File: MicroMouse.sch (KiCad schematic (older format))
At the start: 76 parts, among them CN11 mouseBattery, Q1 IRLML6402, Q2 IRLML6344, SW1 SPST, SW2 SPST, SW3 SPST, U1 FULL_LED_A, U2 STM32F405RGTx, U3 TB6612, U4 CN_MOTOR, U5 CN_MOTOR, U6 MPU9250, U7 ZH

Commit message: とりあえずコミット
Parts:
- removed R10, R9: 10, Resistors_SMD:R_0603_HandSoldering, symbol R
- removed R11: 60.4, Resistors_SMD:R_0603_HandSoldering, symbol R
- removed U1: FULL_LED_A, myfootprint:OSTAMA5B31A, symbol FULL_LED_A
- removed U6: MPU9250, myfootprint:FH-1x5SG, symbol MPU9250
- removed U7: ZH, myfootprint:B6B-ZR, symbol ZH
- added C18, C19, C20, C21: 0.1u, Resistors_SMD:R_0603_HandSoldering, symbol C
- added D1, D2: LED, Resistors_SMD:R_0603_HandSoldering, symbol LED-RESCUE-MicroMouse
- added R2, R3: 280, Resistors_SMD:R_0603_HandSoldering, symbol R
- added U1: 3p, Pin_Headers:Pin_Header_Straight_1x03, symbol 3p
- added U6: 4p, Pin_Headers:Pin_Header_Straight_1x04, symbol 4p
- added U7: icm_left, Pin_Headers:Pin_Header_Straight_1x04, symbol icm_left
- added U8: icm_right, Pin_Headers:Pin_Header_Straight_1x04, symbol icm_right
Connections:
- net labels added: CS, DBG_LED_4, DBG_LED_5, SDO
- net labels removed: Mode_LED_1, Mode_LED_2, Mode_LED_3
- wire segments 289 -> 302
- no-connect marks 28 -> 25
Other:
- note added: "DBG_LED(Orange)"
- note added: "MCU VDD"
- note added: "REG 3.3V"
- note removed: "B"
- note removed: "DBG_LED"
- note removed: "G"
- note removed: "Mode_LED"
- note removed: "O"
- note removed: "Power_IMU"
- note removed: "R"
- note removed: "Y"
- note removed: "YG"
- moved on the sheet: C1, C15, C16, C17, C2, C3, C4, C5, C6, CN11, D13, D5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

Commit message: GNDの配線だけした
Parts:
- removed U7: icm_left, Pin_Headers:Pin_Header_Straight_1x04, symbol icm_left
- removed U8: icm_right, Pin_Headers:Pin_Header_Straight_1x04, symbol icm_right
- added C22: 4.7u, Resistors_SMD:R_0603_HandSoldering, symbol C
- added U7: ICM-20602, myfootprint:ICM-20602, symbol ICM-20602
- C12, C3, C6: footprint myfootprint:EEEHC1E470XP -> Capacitors_SMD:c_elec_6.3x7.7
- CN11: footprint myfootprint:DF3A-2P-2DSA -> RP_KiCAD_Connector:XA_2T
- OPAMP1, OPAMP2: footprint myfootprint:AD8532AR -> Housings_SOIC:SOIC-8_3.9x4.9mm_Pitch1.27mm
- Q1, Q2: footprint myfootprint:IRLML6402 -> myfootprint:SOT-23_Handsoldering
- REG1, REG2: footprint myfootprint:AZ1086 -> TO_SOT_Packages_SMD:SOT-223_reg
- SEN1, SEN2, SEN3, SEN4: footprint myfootprint:TSL262-R-LF-ND -> myfootprint:Socket_Strip_Straight_1x03
- U2: footprint myfootprint:STM32F405RGT6 -> myfootprint:LQFP-64_10x10mm_Pitch0.5mm
- U3: footprint myfootprint:TB6612FNG -> Housings_SSOP:SSOP-24_5.3x8.2mm_Pitch0.65mm
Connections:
- net +3V3: now also C22.1, U7.1 (VDD)
- net CS: now also U7.8 (CS)
- net GND: now also C22.2, U7.5 (GND), U7.7 (NC)
- net SCL: now also U7.2 (SCL/SPC)
- net SDA: now also U7.3 (SDA/SDI)
- net SDO: now also U7.4 (SA0/SDO)

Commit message: 昔の確認
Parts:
- removed C15, C16: 47u, Resistors_SMD:R_1210_HandSoldering, symbol C
- removed C17: 0.1u, Resistors_SMD:R_0603_HandSoldering, symbol C
- removed C3, C6: 47u, Capacitors_SMD:c_elec_6.3x7.7, symbol CP
- added C19: 10u, Resistors_SMD:R_0603_HandSoldering, symbol C
- added C3: 22u, Resistors_SMD:R_0603_HandSoldering, symbol C
- C1, C2: value 47u -> 10u; footprint Resistors_SMD:R_1210_HandSoldering -> Resistors_SMD:R_0603_HandSoldering
- C4: value 47u -> 22u; footprint Resistors_SMD:R_1210_HandSoldering -> Resistors_SMD:R_0603_HandSoldering
- C5: value 47u -> 0.1u; footprint Resistors_SMD:R_1210_HandSoldering -> Resistors_SMD:R_0603_HandSoldering
- renumbered C22 to C10, C7 to C11, C8 to C12, C9 to C13, C10 to C14, C11 to C15, C12 to C16, C13 to C17, C14 to C18, C18 to C6, C19 to C7, C20 to C8, C21 to C9, CN11 to CN1, D5 to D1, D11 to D10, D12 to D11, D6 to D2, D7 to D3, D1 to D4, D2 to D5, D13 to D6, D8 to D7, D9 to D8, D10 to D9, R13 to R10, R15 to R11, R16 to R12, R17 to R13, R18 to R14, R19 to R15, R20 to R16, R21 to R17, R22 to R18, R23 to R19, R6 to R2, R24 to R20, R25 to R21, R26 to R22, R27 to R23, R29 to R24, R28 to R25, R31 to R26, R32 to R27, R7 to R3, R8 to R4, R2 to R5, R3 to R6, R30 to R7, R12 to R8, R14 to R9, U2 to U1, U3 to U2, U4 to U3, U5 to U4, U1 to U5, U7 to U6, U6 to U7
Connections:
- net +3V3: now also C4.1, C5.1, C19.1
- net +5V: now also C3.1; no longer C4.1, C5.1
- net GND: now also C19.2, C3.2

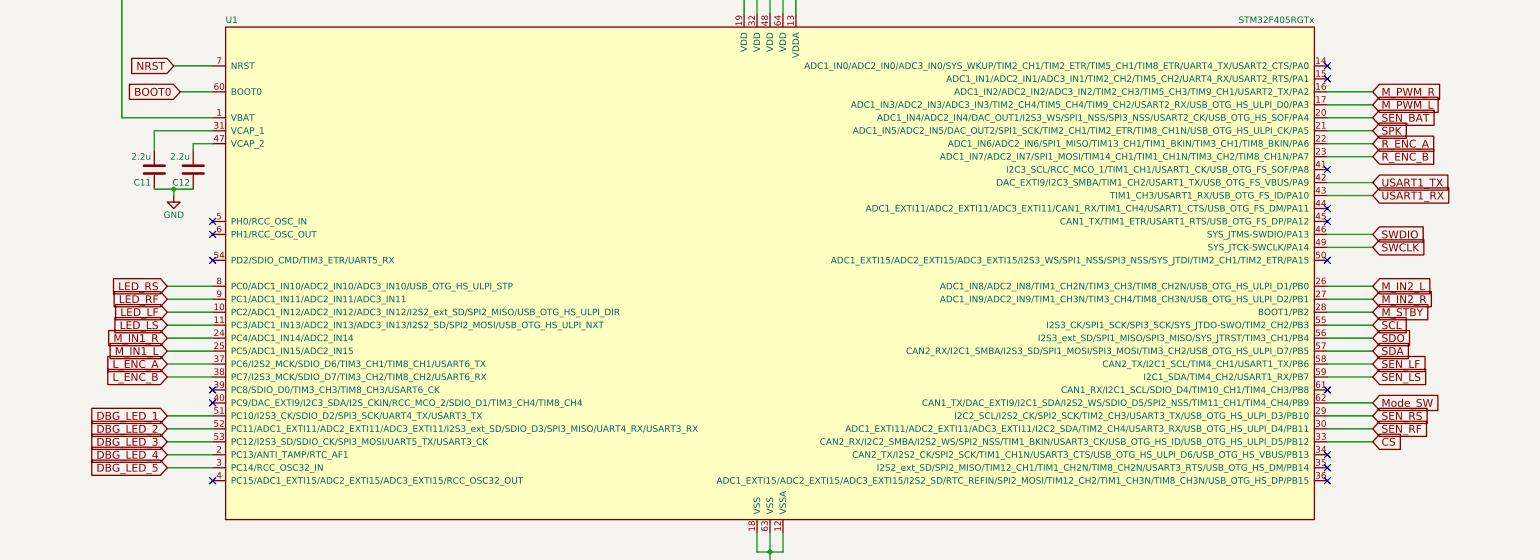
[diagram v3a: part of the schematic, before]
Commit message: stmのピン変え
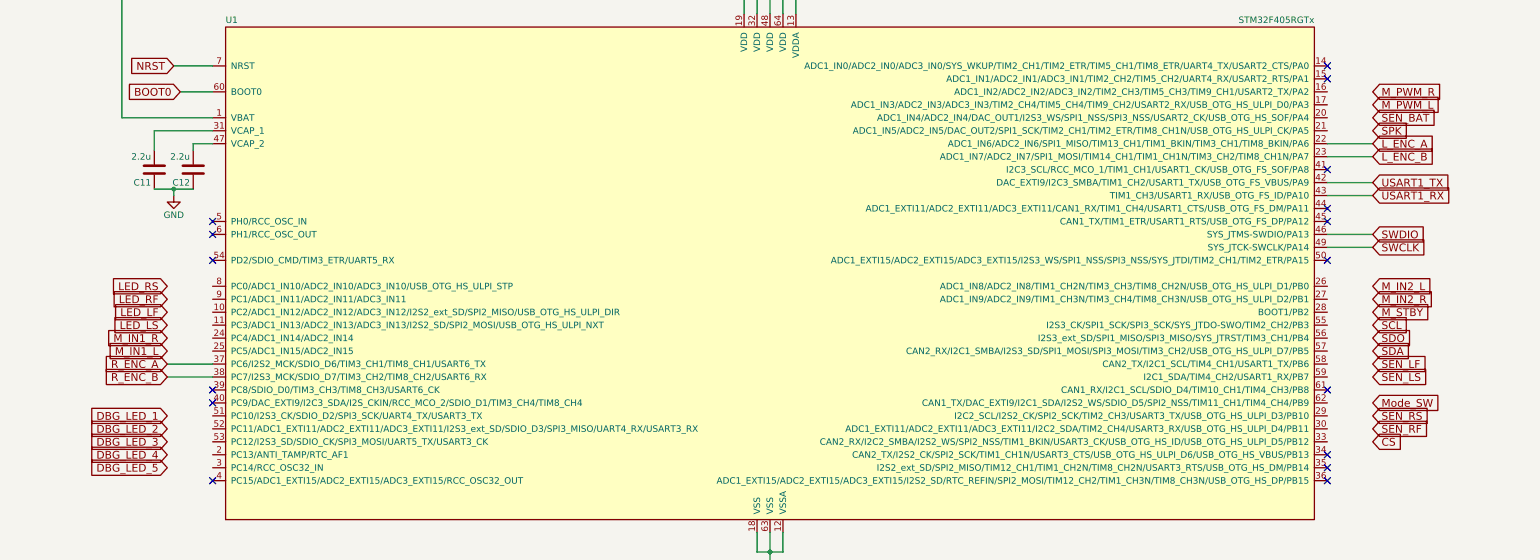
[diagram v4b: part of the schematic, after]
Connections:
- net CS: no longer U1.33 (CAN2_RX/I2C2_SMBA/I2S2_WS/SPI2_NSS/TIM1_BKIN/USART3_CK/USB_OTG_HS_ID/USB_OTG_HS_ULPI_D5/PB12)
- net DBG_LED_1: no longer U1.51 (PC10/I2S3_CK/SDIO_D2/SPI3_SCK/UART4_TX/USART3_TX)
- net DBG_LED_2: no longer U1.52 (PC11/ADC1_EXTI11/ADC2_EXTI11/ADC3_EXTI11/I2S3_ext_SD/SDIO_D3/SPI3_MISO/UART4_RX/USART3_RX)
- net DBG_LED_3: no longer U1.53 (PC12/I2S3_SD/SDIO_CK/SPI3_MOSI/UART5_TX/USART3_CK)
- net DBG_LED_4: no longer U1.2 (PC13/ANTI_TAMP/RTC_AF1)
- net DBG_LED_5: no longer U1.3 (PC14/RCC_OSC32_IN)
- net LED_LF: no longer U1.10 (PC2/ADC1_IN12/ADC2_IN12/ADC3_IN12/I2S2_ext_SD/SPI2_MISO/USB_OTG_HS_ULPI_DIR)
- net LED_LS: no longer U1.11 (PC3/ADC1_IN13/ADC2_IN13/ADC3_IN13/I2S2_SD/SPI2_MOSI/USB_OTG_HS_ULPI_NXT)
- net LED_RF: no longer U1.9 (PC1/ADC1_IN11/ADC2_IN11/ADC3_IN11)
- net LED_RS: no longer U1.8 (PC0/ADC1_IN10/ADC2_IN10/ADC3_IN10/USB_OTG_HS_ULPI_STP)
- net L_ENC_A: now also U1.22 (ADC1_IN6/ADC2_IN6/SPI1_MISO/TIM13_CH1/TIM1_BKIN/TIM3_CH1/TIM8_BKIN/PA6); no longer U1.37 (PC6/I2S2_MCK/SDIO_D6/TIM3_CH1/TIM8_CH1/USART6_TX)
- net L_ENC_B: now also U1.23 (ADC1_IN7/ADC2_IN7/SPI1_MOSI/TIM14_CH1/TIM1_CH1N/TIM3_CH2/TIM8_CH1N/PA7); no longer U1.38 (PC7/I2S3_MCK/SDIO_D7/TIM3_CH2/TIM8_CH2/USART6_RX)
- net M_IN1_L: no longer U1.25 (PC5/ADC1_IN15/ADC2_IN15)
- net M_IN1_R: no longer U1.24 (PC4/ADC1_IN14/ADC2_IN14)
- net M_IN2_L: no longer U1.26 (ADC1_IN8/ADC2_IN8/TIM1_CH2N/TIM3_CH3/TIM8_CH2N/USB_OTG_HS_ULPI_D1/PB0)
- net M_IN2_R: no longer U1.27 (ADC1_IN9/ADC2_IN9/TIM1_CH3N/TIM3_CH4/TIM8_CH3N/USB_OTG_HS_ULPI_D2/PB1)
- net M_PWM_L: no longer U1.17 (ADC1_IN3/ADC2_IN3/ADC3_IN3/TIM2_CH4/TIM5_CH4/TIM9_CH2/USART2_RX/USB_OTG_HS_ULPI_D0/PA3)
- net M_PWM_R: no longer U1.16 (ADC1_IN2/ADC2_IN2/ADC3_IN2/TIM2_CH3/TIM5_CH3/TIM9_CH1/USART2_TX/PA2)
- net M_STBY: no longer U1.28 (BOOT1/PB2)
- net Mode_SW: no longer U1.62 (CAN1_TX/DAC_EXTI9/I2C1_SDA/I2S2_WS/SDIO_D5/SPI2_NSS/TIM11_CH1/TIM4_CH4/PB9)
- net R_ENC_A: now also U1.37 (PC6/I2S2_MCK/SDIO_D6/TIM3_CH1/TIM8_CH1/USART6_TX); no longer U1.22 (ADC1_IN6/ADC2_IN6/SPI1_MISO/TIM13_CH1/TIM1_BKIN/TIM3_CH1/TIM8_BKIN/PA6)
- net R_ENC_B: now also U1.38 (PC7/I2S3_MCK/SDIO_D7/TIM3_CH2/TIM8_CH2/USART6_RX); no longer U1.23 (ADC1_IN7/ADC2_IN7/SPI1_MOSI/TIM14_CH1/TIM1_CH1N/TIM3_CH2/TIM8_CH1N/PA7)
- net SCL: no longer U1.55 (I2S3_CK/SPI1_SCK/SPI3_SCK/SYS_JTDO-SWO/TIM2_CH2/PB3)
- net SDA: no longer U1.57 (CAN2_RX/I2C1_SMBA/I2S3_SD/SPI1_MOSI/SPI3_MOSI/TIM3_CH2/USB_OTG_HS_ULPI_D7/PB5)
- net SDO: no longer U1.56 (I2S3_ext_SD/SPI1_MISO/SPI3_MISO/SYS_JTRST/TIM3_CH1/PB4)
- net SEN_BAT: no longer U1.20 (ADC1_IN4/ADC2_IN4/DAC_OUT1/I2S3_WS/SPI1_NSS/SPI3_NSS/USART2_CK/USB_OTG_HS_SOF/PA4)
- net SEN_LF: no longer U1.58 (CAN2_TX/I2C1_SCL/TIM4_CH1/USART1_TX/PB6)
- net SEN_LS: no longer U1.59 (I2C1_SDA/TIM4_CH2/USART1_RX/PB7)
- net SEN_RF: no longer U1.30 (ADC1_EXTI11/ADC2_EXTI11/ADC3_EXTI11/I2C2_SDA/TIM2_CH4/USART3_RX/USB_OTG_HS_ULPI_D4/PB11)
- net SEN_RS: no longer U1.29 (I2C2_SCL/I2S2_CK/SPI2_SCK/TIM2_CH3/USART3_TX/USB_OTG_HS_ULPI_D3/PB10)
- net SPK: no longer U1.21 (ADC1_IN5/ADC2_IN5/DAC_OUT2/SPI1_SCK/TIM2_CH1/TIM2_ETR/TIM8_CH1N/USB_OTG_HS_ULPI_CK/PA5)
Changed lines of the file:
@@
 	1    0    0    -1
 $EndComp
+Text GLabel 9050 4800 0    60   Input ~ 0
+R_ENC_A
+Text GLabel 9050 4900 0    60   Input ~ 0
+R_ENC_B
 Text GLabel 18350 3100 2    60   Input ~ 0
-R_ENC_A
+L_ENC_A
 Text GLabel 18350 3200 2    60   Input ~ 0
-R_ENC_B
-Text GLabel 9050 4800 0    60   Input ~ 0
-L_ENC_A
-Text GLabel 9050 4900 0    60   Input ~ 0
 L_ENC_B
 Text GLabel 18350 2700 2    60   Input ~ 0
@@
 	15750 9400 16800 9400
 Wire Wire Line
-	9050 4600 9400 4600
-Wire Wire Line
 	7550 9750 7550 10150
 Connection ~ 7550 8650
@@
 Wire Wire Line
 	7550 8050 7550 8250
-Wire Wire Line
-	18000 5100 18350 5100
-Wire Wire Line
-	18000 4900 18350 4900
-Wire Wire Line
-	18000 4800 18350 4800
-Wire Wire Line
-	18000 4400 18350 4400
-Wire Wire Line
-	18000 4300 18350 4300
-Wire Wire Line
-	18000 4200 18350 4200
-Wire Wire Line
-	18000 3000 18350 3000
-Wire Wire Line
-	18000 2900 18350 2900
-Wire Wire Line
-	9050 4900 9400 4900
-Wire Wire Line
-	9050 4800 9400 4800
-Wire Wire Line
-	9050 4500 9400 4500
-Wire Wire Line
-	9050 4400 9400 4400
-Wire Wire Line
-	9050 4300 9400 4300
-Wire Wire Line
-	9050 4200 9400 4200
 Wire Wire Line
 	18000 3500 18350 3500
@@
 	4950 8500 4950 9650
 Wire Wire Line
-	9050 4700 9400 4700
-Wire Wire Line
-	18000 3100 18350 3100
-Wire Wire Line
-	18000 3200 18350 3200
-Wire Wire Line
-	9050 5200 9400 5200
-Wire Wire Line
-	9050 5300 9400 5300
-Wire Wire Line
-	9050 5400 9400 5400
-Wire Wire Line
-	18000 2700 18350 2700
-Wire Wire Line
-	18000 2800 18350 2800
-Wire Wire Line
 	3800 9400 3950 9400
 Wire Wire Line
@@
 Connection ~ 4950 9400
 Wire Wire Line
-	9050 5500 9400 5500
-Wire Wire Line
-	9050 5600 9400 5600
-Wire Wire Line
 	19400 9300 19800 9300
 Wire Wire Line
@@
 Wire Wire Line
 	17950 9550 18400 9550
-Wire Wire Line
-	18000 4500 18350 4500
-Wire Wire Line
-	18000 4600 18350 4600
-Wire Wire Line
-	18000 4700 18350 4700
-Wire Wire Line
-	18000 5200 18350 5200
-Wire Wire Line
-	18000 5300 18350 5300
-Wire Wire Line
-	18000 5400 18350 5400
 Wire Wire Line
 	7600 13850 7600 13700
@@
 	1    0    0    -1
 $EndComp
+Wire Wire Line
+	9050 4800 9400 4800
+Wire Wire Line
+	9050 4900 9400 4900
+Wire Wire Line
+	18000 3100 18350 3100
+Wire Wire Line
+	18000 3200 18350 3200
 $EndSCHEMATC

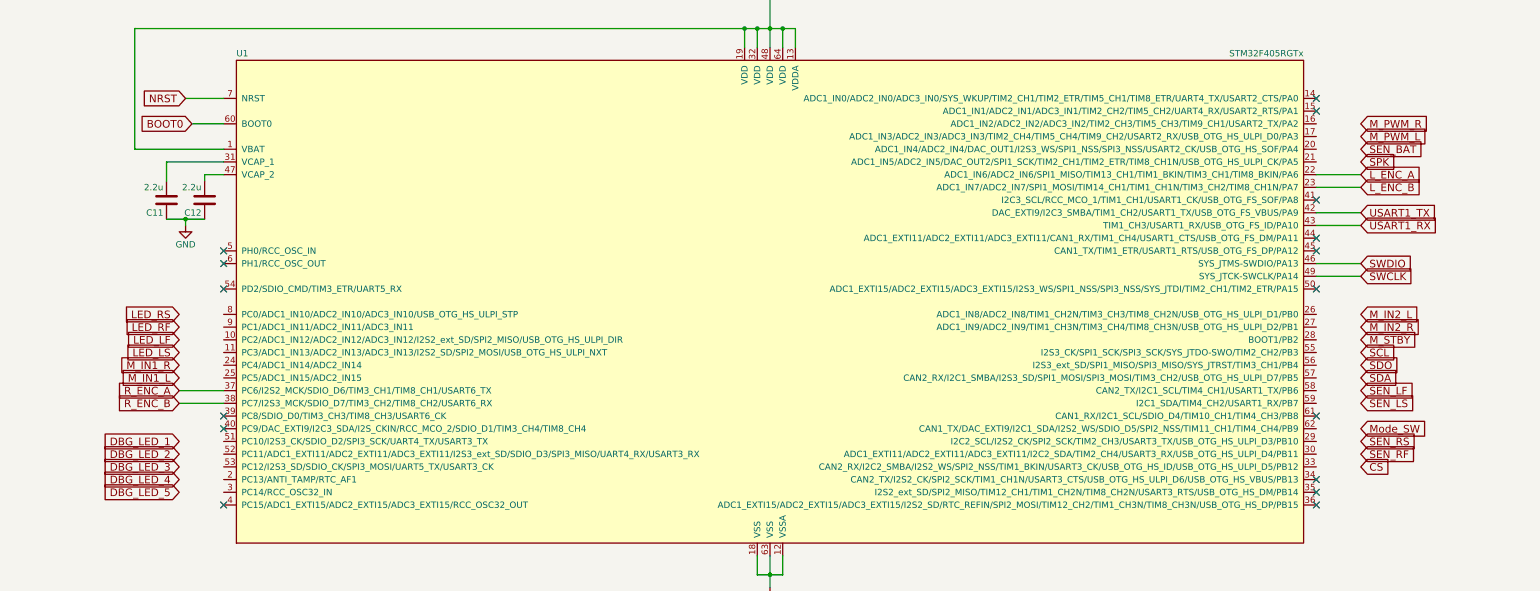
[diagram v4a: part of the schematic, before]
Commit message: ピン変えました
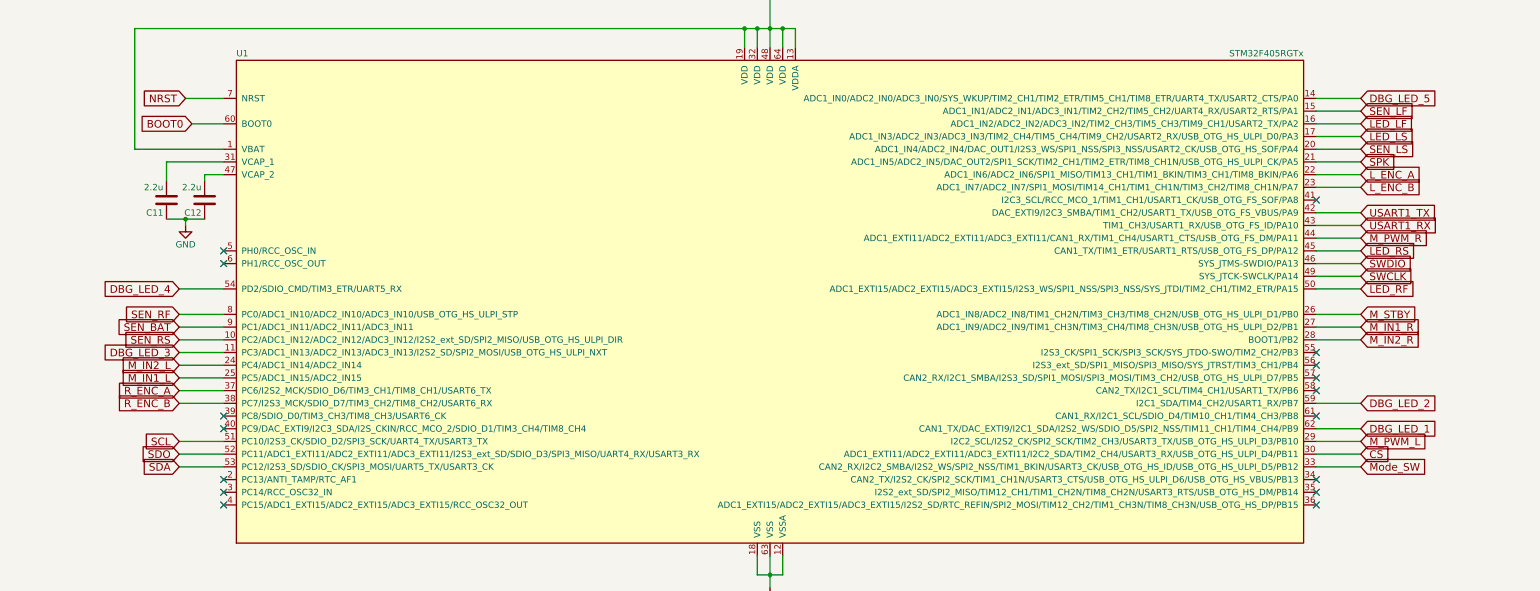
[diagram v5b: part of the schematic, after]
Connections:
- net CS: now also U1.30 (ADC1_EXTI11/ADC2_EXTI11/ADC3_EXTI11/I2C2_SDA/TIM2_CH4/USART3_RX/USB_OTG_HS_ULPI_D4/PB11)
- net DBG_LED_1: now also U1.62 (CAN1_TX/DAC_EXTI9/I2C1_SDA/I2S2_WS/SDIO_D5/SPI2_NSS/TIM11_CH1/TIM4_CH4/PB9)
- net DBG_LED_2: now also U1.59 (I2C1_SDA/TIM4_CH2/USART1_RX/PB7)
- net DBG_LED_3: now also U1.11 (PC3/ADC1_IN13/ADC2_IN13/ADC3_IN13/I2S2_SD/SPI2_MOSI/USB_OTG_HS_ULPI_NXT)
- net DBG_LED_4: now also U1.54 (PD2/SDIO_CMD/TIM3_ETR/UART5_RX)
- net DBG_LED_5: now also U1.14 (ADC1_IN0/ADC2_IN0/ADC3_IN0/SYS_WKUP/TIM2_CH1/TIM2_ETR/TIM5_CH1/TIM8_ETR/UART4_TX/USART2_CTS/PA0)
- net LED_LF: now also U1.16 (ADC1_IN2/ADC2_IN2/ADC3_IN2/TIM2_CH3/TIM5_CH3/TIM9_CH1/USART2_TX/PA2)
- net LED_LS: now also U1.17 (ADC1_IN3/ADC2_IN3/ADC3_IN3/TIM2_CH4/TIM5_CH4/TIM9_CH2/USART2_RX/USB_OTG_HS_ULPI_D0/PA3)
- net LED_RF: now also U1.50 (ADC1_EXTI15/ADC2_EXTI15/ADC3_EXTI15/I2S3_WS/SPI1_NSS/SPI3_NSS/SYS_JTDI/TIM2_CH1/TIM2_ETR/PA15)
- net LED_RS: now also U1.45 (CAN1_TX/TIM1_ETR/USART1_RTS/USB_OTG_FS_DP/PA12)
- net M_IN1_L: now also U1.25 (PC5/ADC1_IN15/ADC2_IN15)
- net M_IN1_R: now also U1.27 (ADC1_IN9/ADC2_IN9/TIM1_CH3N/TIM3_CH4/TIM8_CH3N/USB_OTG_HS_ULPI_D2/PB1)
- net M_IN2_L: now also U1.24 (PC4/ADC1_IN14/ADC2_IN14)
- net M_IN2_R: now also U1.28 (BOOT1/PB2)
- net M_PWM_L: now also U1.29 (I2C2_SCL/I2S2_CK/SPI2_SCK/TIM2_CH3/USART3_TX/USB_OTG_HS_ULPI_D3/PB10)
- net M_PWM_R: now also U1.44 (ADC1_EXTI11/ADC2_EXTI11/ADC3_EXTI11/CAN1_RX/TIM1_CH4/USART1_CTS/USB_OTG_FS_DM/PA11)
- net M_STBY: now also U1.26 (ADC1_IN8/ADC2_IN8/TIM1_CH2N/TIM3_CH3/TIM8_CH2N/USB_OTG_HS_ULPI_D1/PB0)
- net Mode_SW: now also U1.33 (CAN2_RX/I2C2_SMBA/I2S2_WS/SPI2_NSS/TIM1_BKIN/USART3_CK/USB_OTG_HS_ID/USB_OTG_HS_ULPI_D5/PB12)
- net SCL: now also U1.51 (PC10/I2S3_CK/SDIO_D2/SPI3_SCK/UART4_TX/USART3_TX)
- net SDA: now also U1.53 (PC12/I2S3_SD/SDIO_CK/SPI3_MOSI/UART5_TX/USART3_CK)
- net SDO: now also U1.52 (PC11/ADC1_EXTI11/ADC2_EXTI11/ADC3_EXTI11/I2S3_ext_SD/SDIO_D3/SPI3_MISO/UART4_RX/USART3_RX)
- net SEN_BAT: now also U1.9 (PC1/ADC1_IN11/ADC2_IN11/ADC3_IN11)
- net SEN_LF: now also U1.15 (ADC1_IN1/ADC2_IN1/ADC3_IN1/TIM2_CH2/TIM5_CH2/UART4_RX/USART2_RTS/PA1)
- net SEN_LS: now also U1.20 (ADC1_IN4/ADC2_IN4/DAC_OUT1/I2S3_WS/SPI1_NSS/SPI3_NSS/USART2_CK/USB_OTG_HS_SOF/PA4)
- net SEN_RF: now also U1.8 (PC0/ADC1_IN10/ADC2_IN10/ADC3_IN10/USB_OTG_HS_ULPI_STP)
- net SEN_RS: now also U1.10 (PC2/ADC1_IN12/ADC2_IN12/ADC3_IN12/I2S2_ext_SD/SPI2_MISO/USB_OTG_HS_ULPI_DIR)
- net SPK: now also U1.21 (ADC1_IN5/ADC2_IN5/DAC_OUT2/SPI1_SCK/TIM2_CH1/TIM2_ETR/TIM8_CH1N/USB_OTG_HS_ULPI_CK/PA5)

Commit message: kicadアップデートマン
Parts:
- D10, D11, D8, D9: footprint LEDs:LED-5MM -> myfootprint:LED-5MM
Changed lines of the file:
@@
 F 0 "D11" H 12150 13150 50  0000 C CNN
 F 1 "LED_LF" H 12150 12950 50  0000 C CNN
-F 2 "LEDs:LED-5MM" H 12150 13050 50  0001 C CNN
+F 2 "myfootprint:LED-5MM" H 12150 13050 50  0001 C CNN
 F 3 "" H 12150 13050 50  0000 C CNN
 	1    12150 13050
@@
 F 0 "D9" H 10500 13150 50  0000 C CNN
 F 1 "LED_LS" H 10500 12950 50  0000 C CNN
-F 2 "LEDs:LED-5MM" H 10500 13050 50  0001 C CNN
+F 2 "myfootprint:LED-5MM" H 10500 13050 50  0001 C CNN
 F 3 "" H 10500 13050 50  0000 C CNN
 	1    10500 13050
@@
 F 0 "D10" H 12150 10950 50  0000 C CNN
 F 1 "LED_RF" H 12150 10750 50  0000 C CNN
-F 2 "LEDs:LED-5MM" H 12150 10850 50  0001 C CNN
+F 2 "myfootprint:LED-5MM" H 12150 10850 50  0001 C CNN
 F 3 "" H 12150 10850 50  0000 C CNN
 	1    12150 10850
@@
 F 0 "D8" H 10500 10950 50  0000 C CNN
 F 1 "LED_RS" H 10500 10750 50  0000 C CNN
-F 2 "LEDs:LED-5MM" H 10500 10850 50  0001 C CNN
+F 2 "myfootprint:LED-5MM" H 10500 10850 50  0001 C CNN
 F 3 "" H 10500 10850 50  0000 C CNN
 	1    10500 10850

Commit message: あとはビアの調整
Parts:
- C1, C10, C11, C12, C13, C14, C15, C17, C18, C19, C2, C3, C4, C5, C6, C7, C8, C9: symbol C -> device:C
- C16: symbol CP -> device:CP
- CN1: symbol mouseBattery -> mouseBattery:mouseBattery
- D1, D10, D11, D2, D3, D4, D5, D6, D7, D8, D9: symbol LED-RESCUE-MicroMouse -> MicroMouse-rescue:LED-RESCUE-MicroMouse
- OPAMP1, OPAMP2: symbol AD8532AR -> ad8532ar:AD8532AR
- Q1: symbol IRLML6402 -> nosuz:IRLML6402
- Q2: symbol IRLML6344 -> nosuz:IRLML6344
- R1, R10, R11, R12, R13, R14, R15, R16, R17, R18, R19, R2, R20, R21, R22, R23, R24, R25, R26, R27, R3, R4, R5, R6, R7, R8, R9: symbol R -> device:R
- REG1, REG2: symbol AZ1086 -> az1086:AZ1086
- SEN1, SEN2, SEN3, SEN4: symbol TSL262R -> tsl262r:TSL262R
- SP1: symbol SPEAKER -> MicroMouse-rescue:SPEAKER
- SW1, SW2, SW3: symbol SPST -> MicroMouse-rescue:SPST
- U1: symbol STM32F405RGTx -> MCU_ST_STM32:STM32F405RGTx
- U2: symbol TB6612 -> tb6612:TB6612
- U3, U4: symbol CN_MOTOR -> cn_motor:CN_MOTOR
- U5: symbol 3p -> 3p:3p
- U6: symbol ICM-20602 -> icm-20602:ICM-20602
- U7: symbol 4p -> 4p:4p
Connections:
- net +3V3: no longer R2.1, R3.1, R4.1, R5.1, R6.1
- net DBG_LED_1: now also R2.2; no longer D1.1 (K)
- net DBG_LED_2: now also R3.2; no longer D2.1 (K)
- net DBG_LED_3: now also R4.2; no longer D3.1 (K)
- net DBG_LED_4: now also R5.2; no longer D4.1 (K)
- net DBG_LED_5: now also R6.2; no longer D5.1 (K)
- net GND: now also D1.1 (K), D2.1 (K), D3.1 (K), D4.1 (K), D5.1 (K); no longer C6.2
- net at D1.2 (A): now also R2.1; no longer R2.2
- net at D2.2 (A): now also R3.1; no longer R3.2
- net at D3.2 (A): now also R4.1; no longer R4.2
- net at D4.2 (A): now also R5.1; no longer R5.2
- net at D5.2 (A): now also R6.1; no longer R6.2
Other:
- moved on the sheet: D1, D2, D3, D4, D5, R2, R3, R4, R5, R6
